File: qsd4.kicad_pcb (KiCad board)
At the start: 2 copper layers, 100 x 75 mm, 66 parts, among them J1 5-1814832-1, J2 5-1814832-1, J3 Conn_02x08_Odd_Even, J4 SJ-3524-SMT, U10 GALI-39, U3 SN74CBT3253, U4 SN74AC74PW, U5 AD8226ARZ-R7, U6 AD8226ARZ-R7, U7 AP2120N-2.5TRG1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

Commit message: Push to github.
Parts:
- C12, C14: value 3300pF -> 2200pF
- moved R32 0.68 mm to (135.1, 64.3)
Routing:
- net Net-(U3-1A): track 6.02 -> 5.28 mm
- net GND: vias 92 -> 93
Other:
- board text added: "CLK IN"

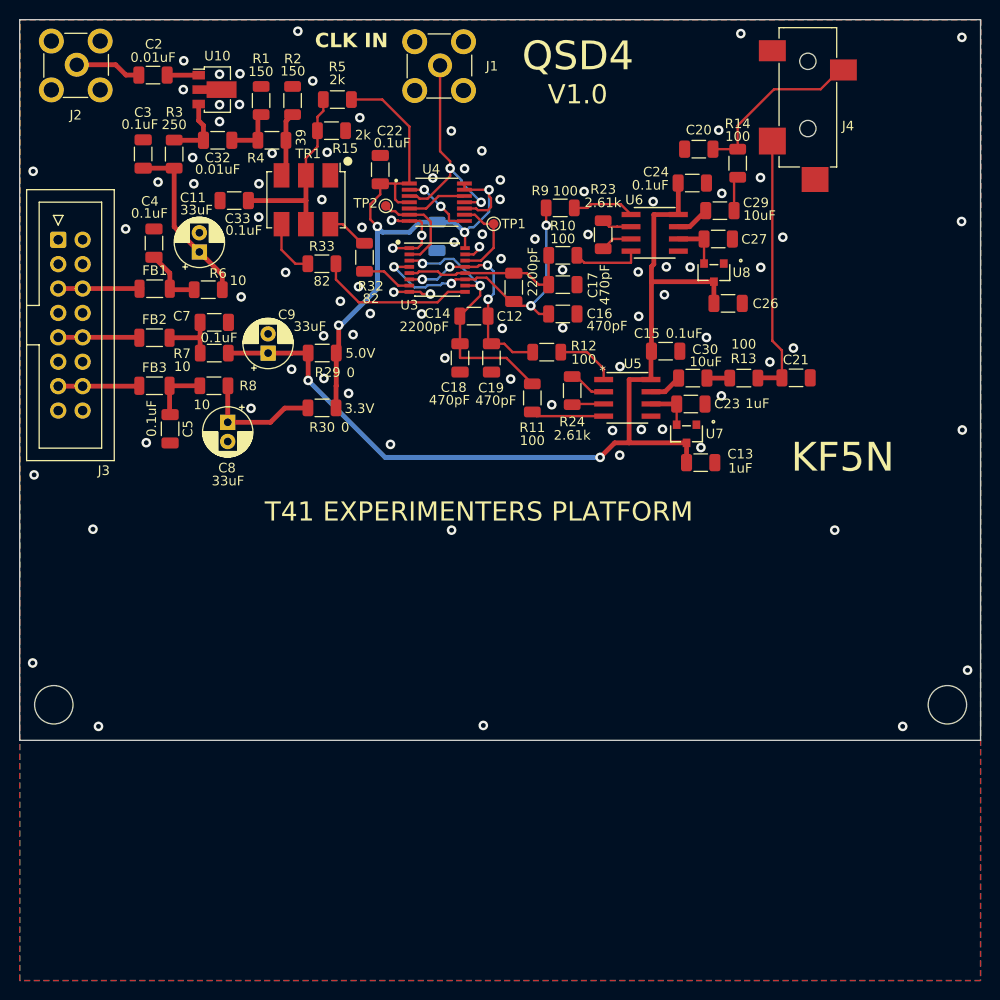
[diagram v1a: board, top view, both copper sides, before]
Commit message: Version 1.1 PCB for the QSD4.  Documentation updated.
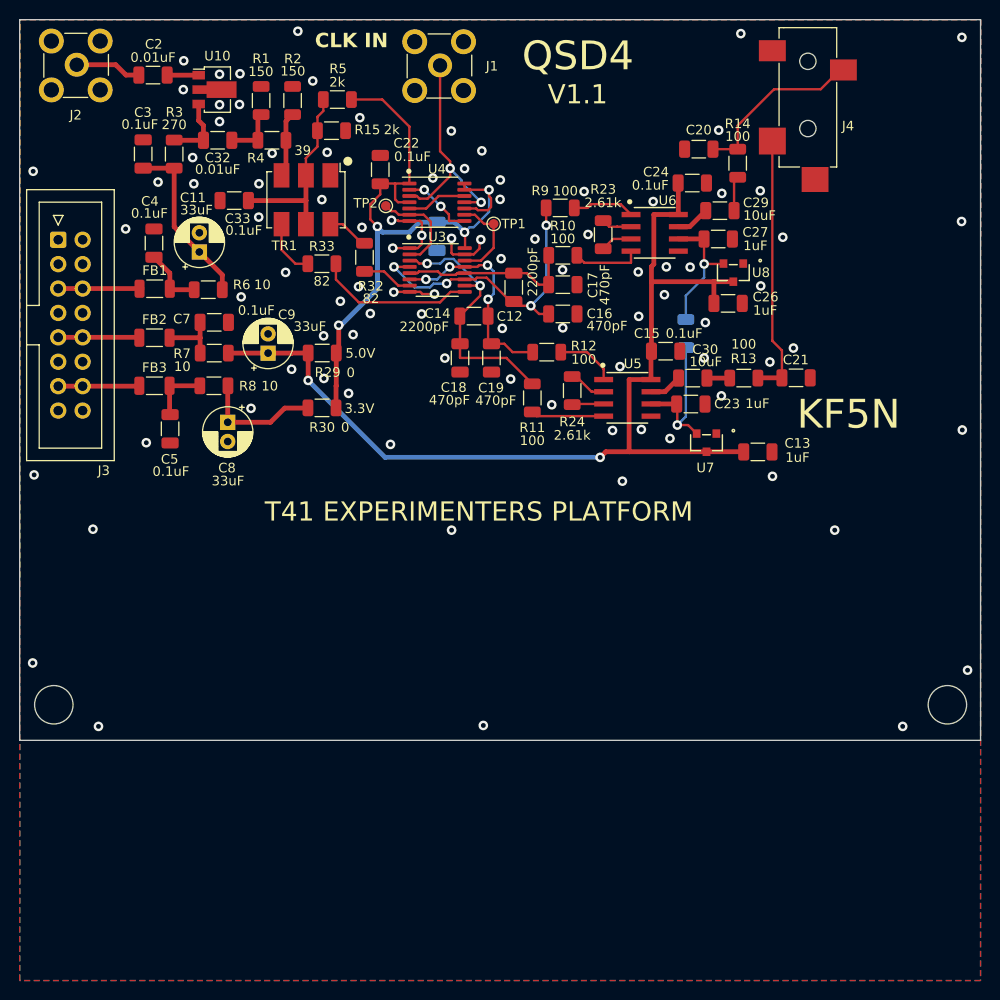
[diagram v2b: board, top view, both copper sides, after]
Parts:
- added R16: 0, Resistor_SMD:R_1206_3216Metric, B.Cu at (168.5, 72.3)
- C20, C21: value 1nF -> ~
- R3: value 250 -> 270
- U3: footprint Package_SO:SSOP-16_4.4x5.2mm_P0.65mm -> Package_SO:TSSOP-16_4.4x5mm_P0.65mm
- U4: footprint SN74AC74PW:SOP65P640X120-14N -> Package_SO:TSSOP-14_4.4x5mm_P0.65mm
- moved C13 6.05 mm to (176.0, 84.6)
- moved U7 2.28 mm to (170.7, 83.6)
- moved U8 2.02 mm to (173.5, 65.9)
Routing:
- net /REF_I: track 4.83 -> 15.8 mm, vias 0 -> 1
- net /REF_Q: track 5.23 -> 13.9 mm, vias 0 -> 1
- net /5V_FILT: track 97.5 -> 104.0 mm
- net GND: track 14.6 -> 18.4 mm
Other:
- board text added: "V1.1"
- board text removed: "V1.0"
